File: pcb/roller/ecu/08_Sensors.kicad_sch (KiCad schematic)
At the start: 40 parts, among them Q4 BC817, U7 SN74LVC1G14DBV

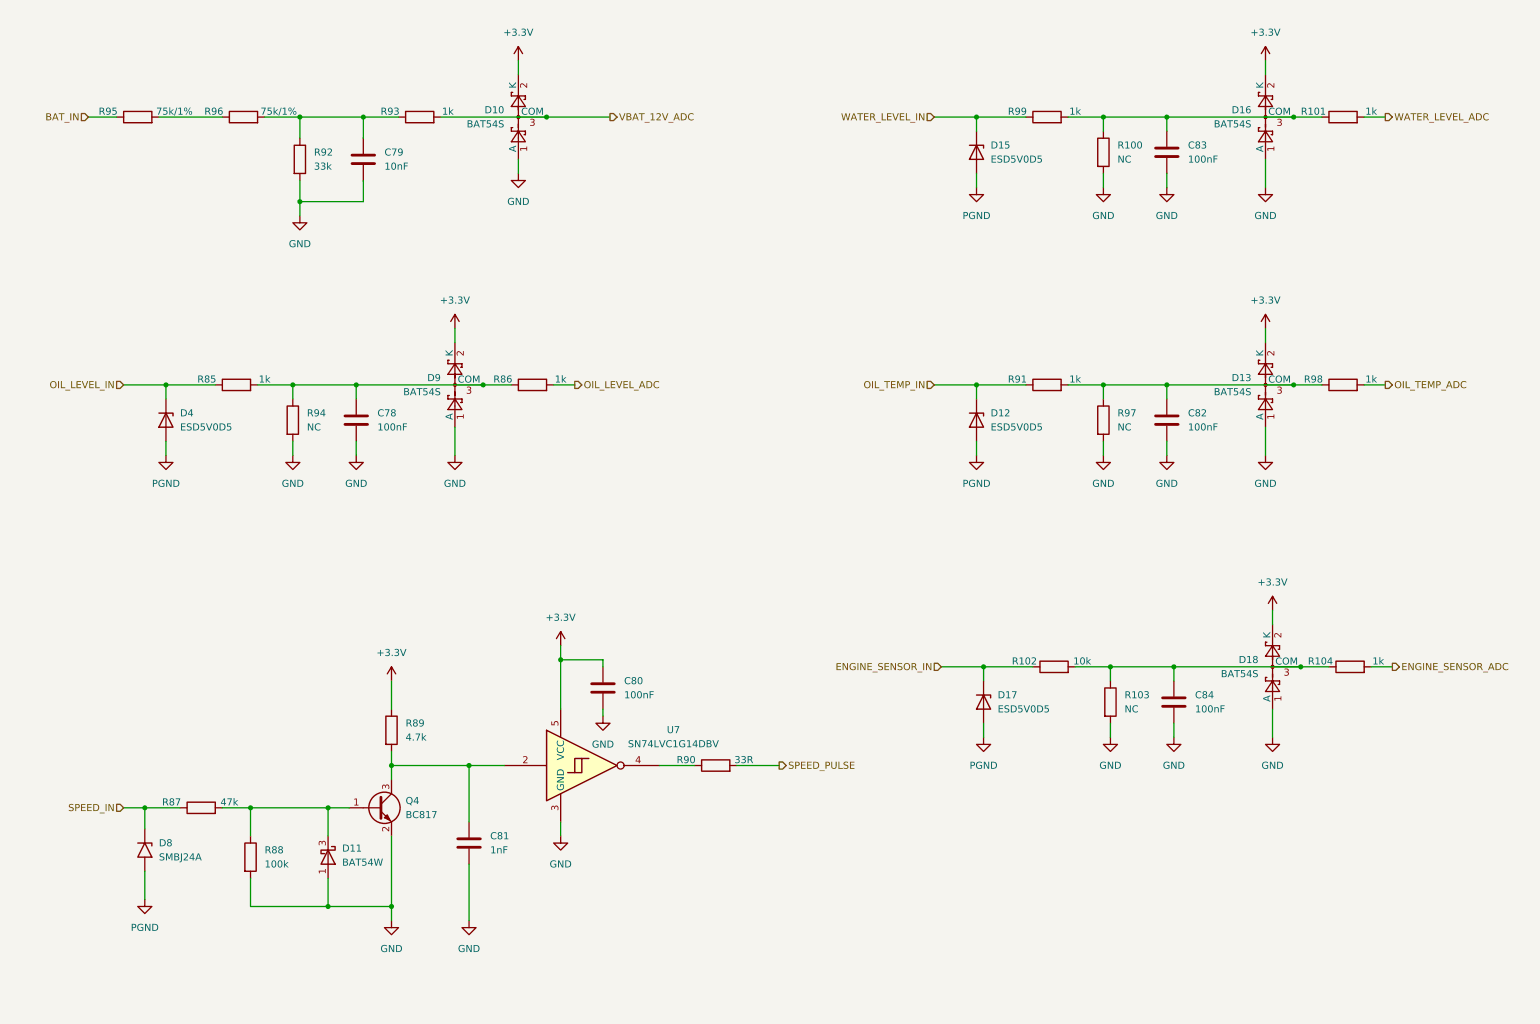
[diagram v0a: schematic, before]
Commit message: Add ESTOP_NC pin and wire connections in ECU schematic; update designators in PCB project
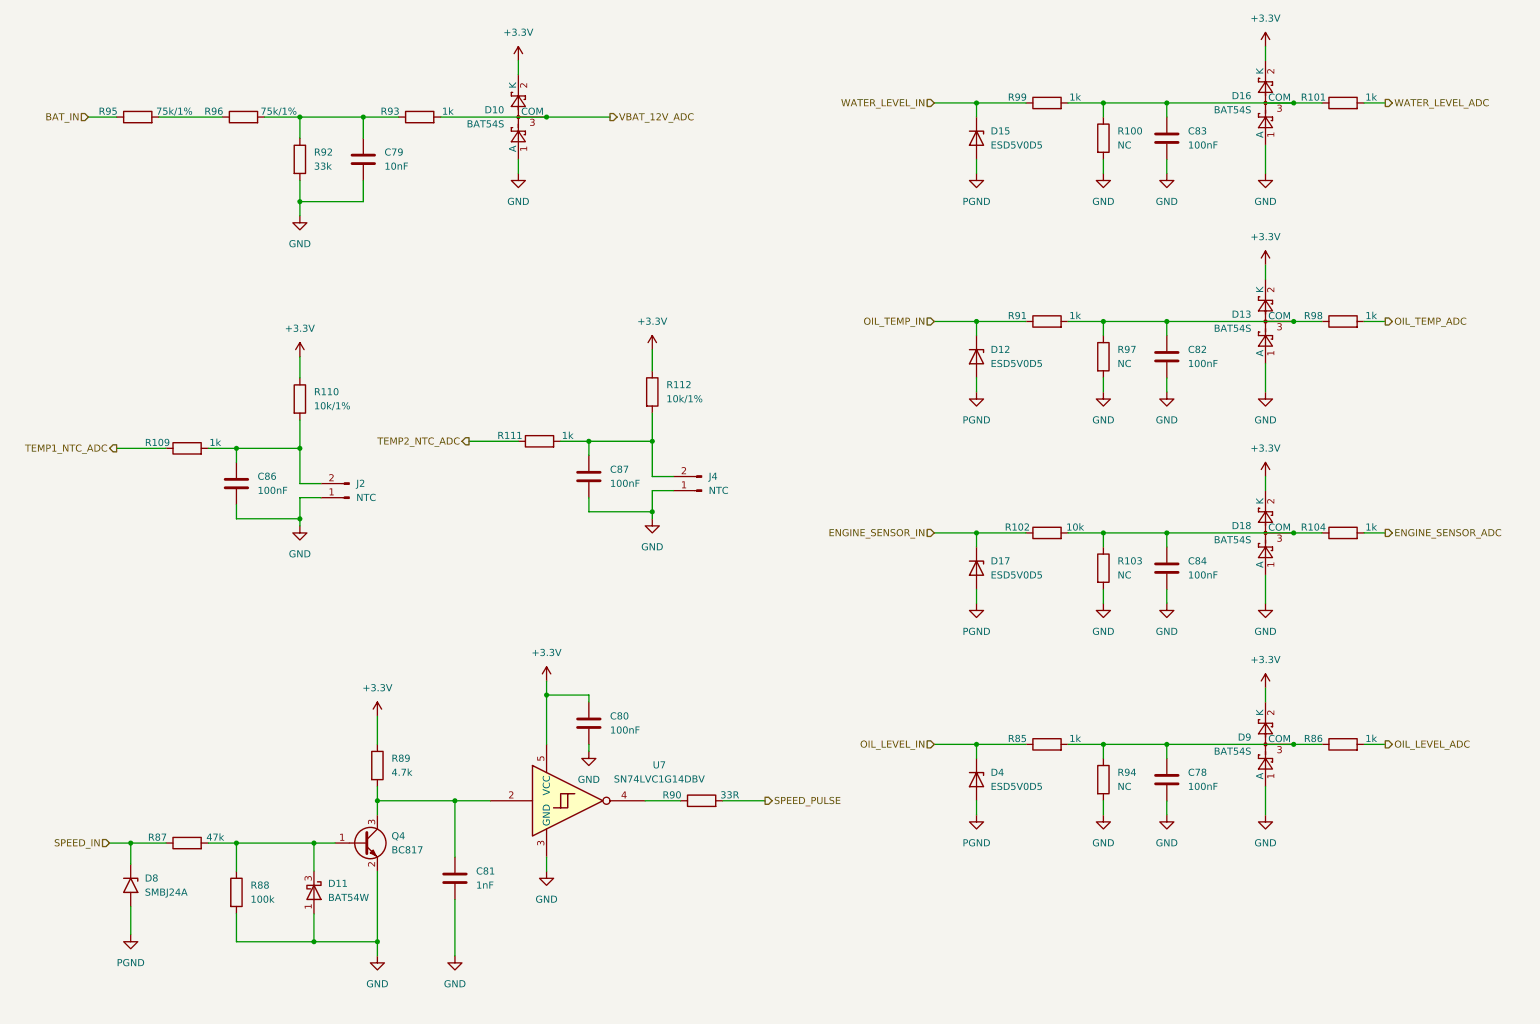
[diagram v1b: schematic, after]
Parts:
- added C86, C87: 100nF, Capacitor_SMD:C_0603_1608Metric, symbol Device:C
- added J2, J4: NTC, Connector_PinHeader_2.54mm:PinHeader_1x02_P2.54mm_Vertical, symbol Connector:Conn_01x02_Pin
- added R109, R111: 1k, Resistor_SMD:R_0603_1608Metric, symbol Device:R
- added R110, R112: 10k/1%, Resistor_SMD:R_0603_1608Metric, symbol Device:R
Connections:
- net +3.3V: now also R110.1, R112.1
- net GND: now also C86.2, C87.2, J2.1 (Pin_1), J4.1 (Pin_1)
- new net: C87.1, J4.2 (Pin_2), R111.2, R112.2
- new net: C86.1, J2.2 (Pin_2), R109.2, R110.2
- new net TEMP1_NTC_ADC: R109.1
- new net TEMP2_NTC_ADC: R111.1
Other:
- moved on the sheet: C78, C80, C81, C82, C83, C84, D11, D12, D13, D15, D16, D17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

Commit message: Refactor ECU schematic and project files
- Updated used designators in ecu.kicad_pro to reflect current components.
- Adjusted wire connections in ecu.kicad_sch for better layout and clarity.
- Added new wires and labels for ESTOP functionality.
- Modified pin placements and sizes for improved organization in the schematic.
- Ensured all changes maintain compatibility with existing design specifications.
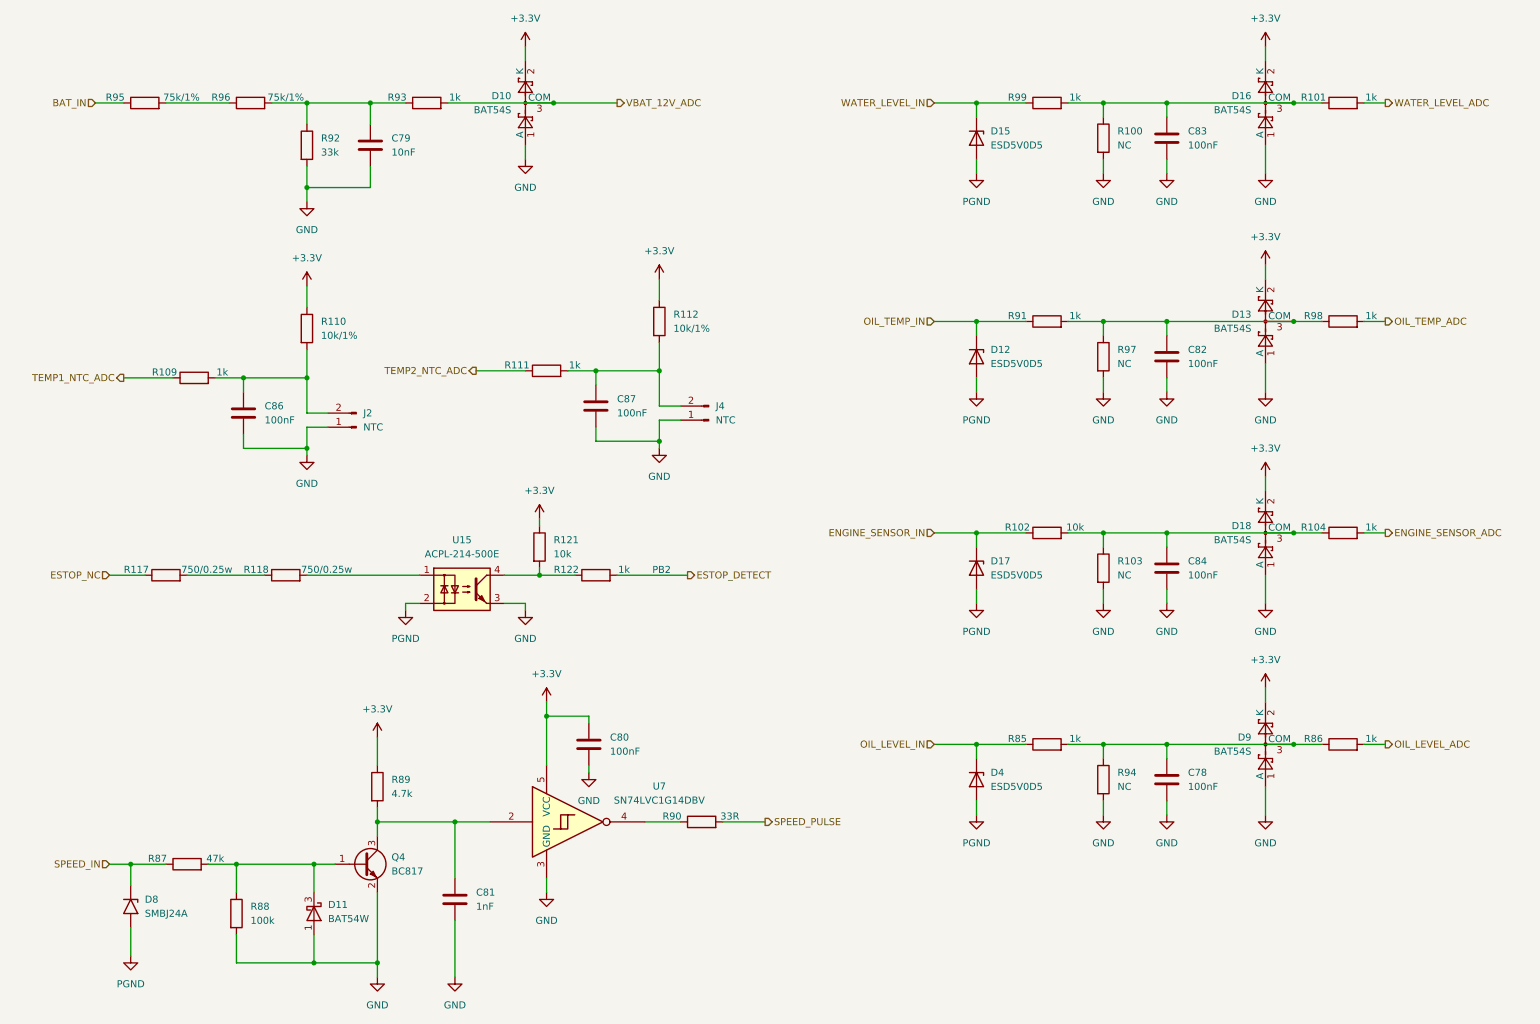
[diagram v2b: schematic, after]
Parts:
- added R117, R118: 750/0.25w, Resistor_SMD:R_1206_3216Metric, symbol Device:R
- added R121: 10k, Resistor_SMD:R_0603_1608Metric, symbol Device:R
- added R122: 1k, Resistor_SMD:R_0603_1608Metric, symbol Device:R
- added U15: ACPL-214-500E, Package_SO:SOP-4_4.4x2.6mm_P1.27mm, symbol Isolator:ACPL-214-500E
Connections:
- net +3.3V: now also R121.1
- net GND: now also U15.3
- net PGND: now also U15.2
- new net: R117.2, R118.1
- new net: R118.2, U15.1
- new net: R121.2, R122.1, U15.4
- new net ESTOP_DETECT: R122.2
- new net ESTOP_NC: R117.1
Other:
- note added: "PB2"
- moved on the sheet: C79, C80, C81, C86, C87, D10, D11, D8, J2, J4, Q4, R109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
